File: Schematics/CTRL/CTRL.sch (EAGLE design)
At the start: 50 parts

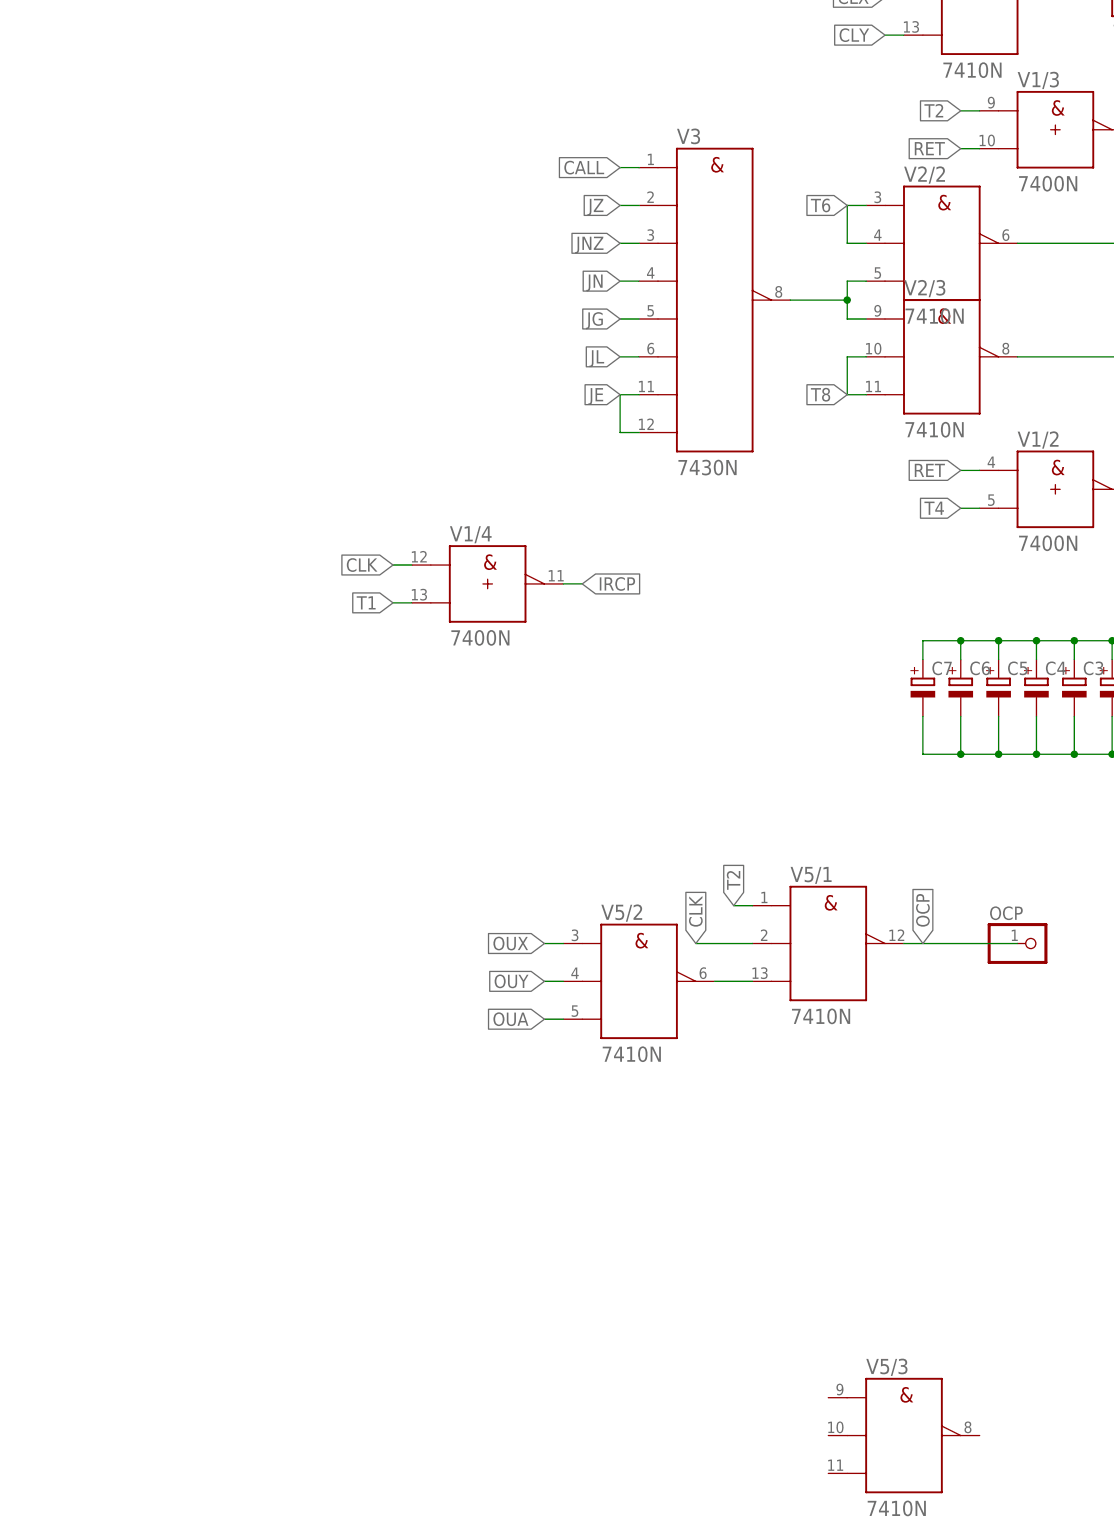
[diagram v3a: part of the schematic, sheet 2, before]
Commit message: Fixed problem with 0xXX
RET wasnt negated, 0xFF and 0xFE started to over heat when T2 was High.
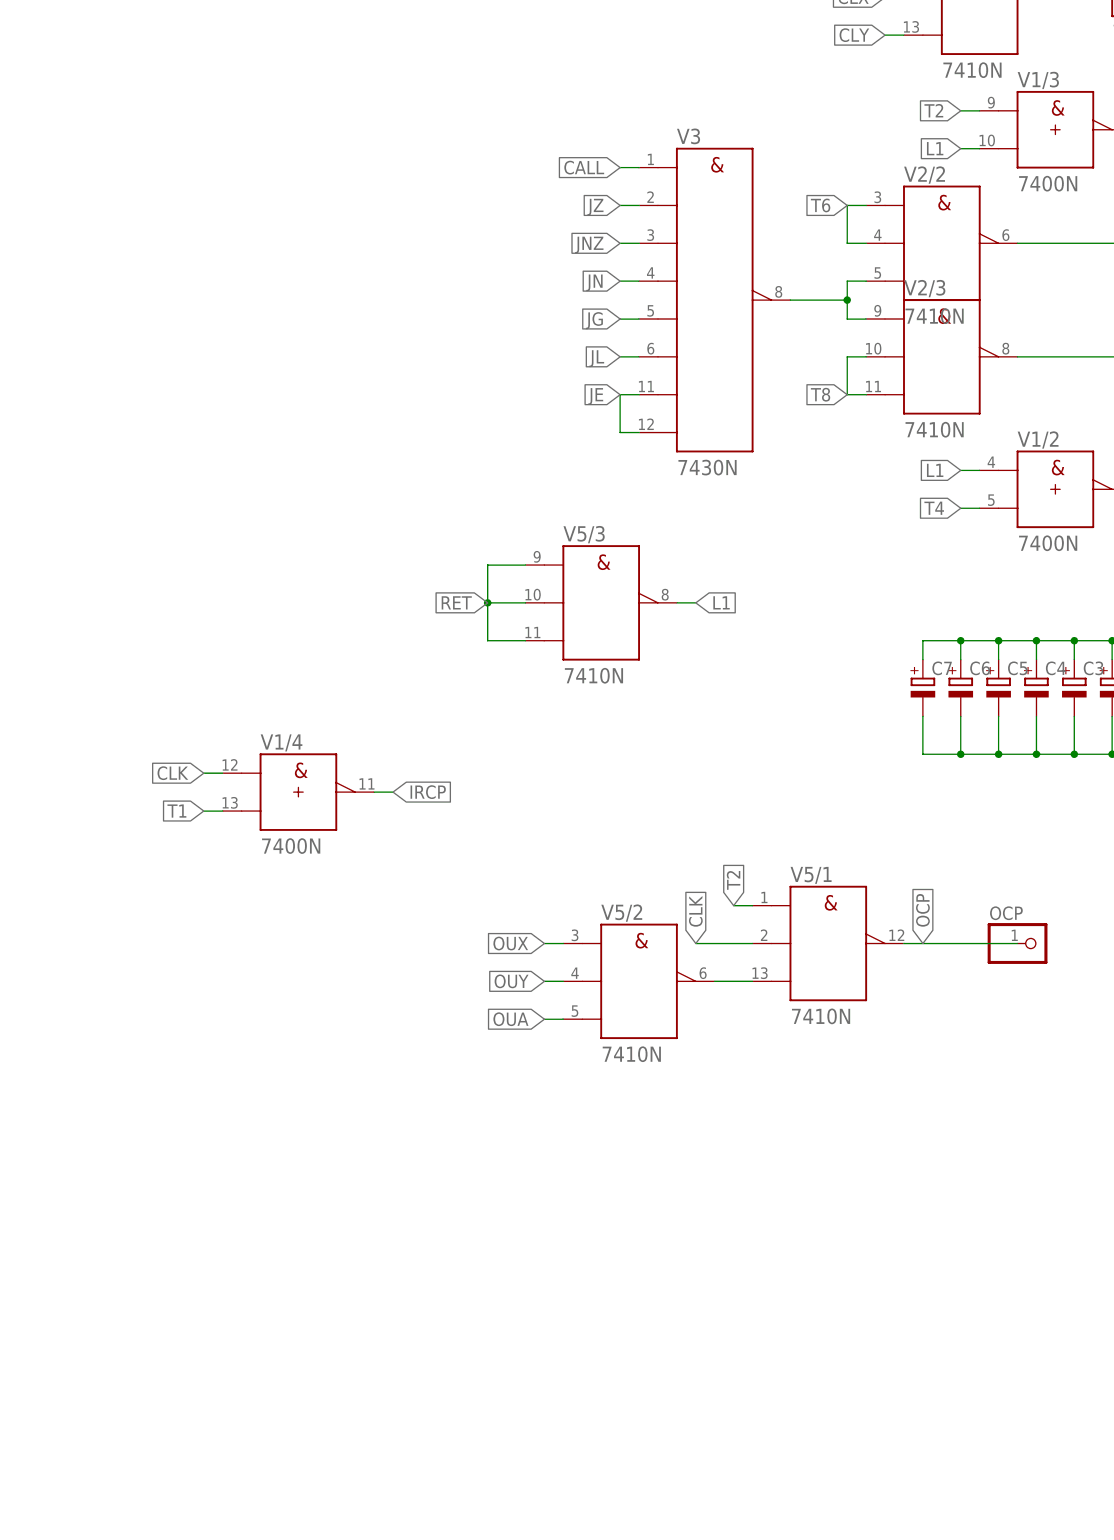
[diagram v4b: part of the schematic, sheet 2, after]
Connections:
- new net L1: V1/2.A, V1/3.B, V5/3.Y
- net RET: now also V5/3.A, V5/3.B, V5/3.C; no longer V1/2.A, V1/3.B
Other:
- moved on the sheet: V1/4, V5/3
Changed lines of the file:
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@@
 <attribute name="VALUE" x="327.66" y="217.805" size="2.032" layer="96"/>
 </instance>
-<instance part="V1" gate="/4" x="256.54" y="165.1" smashed="yes">
-<attribute name="NAME" x="251.46" y="170.815" size="2.032" layer="95"/>
-<attribute name="VALUE" x="251.46" y="156.845" size="2.032" layer="96"/>
+<instance part="V1" gate="/4" x="231.14" y="137.16" smashed="yes">
+<attribute name="NAME" x="226.06" y="142.875" size="2.032" layer="95"/>
+<attribute name="VALUE" x="226.06" y="128.905" size="2.032" layer="96"/>
 </instance>
 <instance part="V2" gate="/1" x="322.58" y="243.84" smashed="yes">
@@
 <attribute name="VALUE" x="271.78" y="100.965" size="2.032" layer="96"/>
 </instance>
-<instance part="V5" gate="/3" x="312.42" y="50.8" smashed="yes">
-<attribute name="NAME" x="307.34" y="59.055" size="2.032" layer="95"/>
-<attribute name="VALUE" x="307.34" y="40.005" size="2.032" layer="96"/>
+<instance part="V5" gate="/3" x="271.78" y="162.56" smashed="yes">
+<attribute name="NAME" x="266.7" y="170.815" size="2.032" layer="95"/>
+<attribute name="VALUE" x="266.7" y="151.765" size="2.032" layer="96"/>
 </instance>
 <instance part="OCP" gate="G$1" x="330.2" y="116.84" smashed="yes">
@@
 <net name="RET" class="0">
 <segment>
-<pinref part="V1" gate="/3" pin="B"/>
-<wire x1="320.04" y1="223.52" x2="322.58" y2="223.52" width="0.1524" layer="91"/>
-<label x="320.04" y="223.52" size="1.778" layer="95" rot="R180" xref="yes"/>
-</segment>
-<segment>
-<pinref part="V1" gate="/2" pin="A"/>
-<wire x1="320.04" y1="180.34" x2="322.58" y2="180.34" width="0.1524" layer="91"/>
-<label x="320.04" y="180.34" size="1.778" layer="95" rot="R180" xref="yes"/>
-</segment>
-<segment>
 <wire x1="63.5" y1="152.4" x2="58.42" y2="152.4" width="0.1524" layer="91"/>
 <pinref part="RAM-OP" gate="A" pin="6"/>
@@
 <pinref part="PC-OP0" gate="A" pin="13"/>
 <label x="129.54" y="147.32" size="1.778" layer="95" xref="yes"/>
+</segment>
+<segment>
+<pinref part="V5" gate="/3" pin="B"/>
+<pinref part="V5" gate="/3" pin="C"/>
+<wire x1="261.62" y1="157.48" x2="256.54" y2="157.48" width="0.1524" layer="91"/>
+<wire x1="256.54" y1="157.48" x2="256.54" y2="162.56" width="0.1524" layer="91"/>
+<pinref part="V5" gate="/3" pin="A"/>
+<wire x1="256.54" y1="162.56" x2="256.54" y2="167.64" width="0.1524" layer="91"/>
+<wire x1="256.54" y1="167.64" x2="261.62" y2="167.64" width="0.1524" layer="91"/>
+<wire x1="261.62" y1="162.56" x2="256.54" y2="162.56" width="0.1524" layer="91"/>
+<junction x="256.54" y="162.56"/>
+<label x="256.54" y="162.56" size="1.778" layer="95" rot="R180" xref="yes"/>
 </segment>
 </net>
@@
 <segment>
 <pinref part="V1" gate="/4" pin="A"/>
-<wire x1="243.84" y1="167.64" x2="246.38" y2="167.64" width="0.1524" layer="91"/>
-<label x="243.84" y="167.64" size="1.778" layer="95" rot="R180" xref="yes"/>
+<wire x1="218.44" y1="139.7" x2="220.98" y2="139.7" width="0.1524" layer="91"/>
+<label x="218.44" y="139.7" size="1.778" layer="95" rot="R180" xref="yes"/>
 </segment>
 <segment>
@@
 <segment>
 <pinref part="V1" gate="/4" pin="B"/>
-<wire x1="243.84" y1="162.56" x2="246.38" y2="162.56" width="0.1524" layer="91"/>
-<label x="243.84" y="162.56" size="1.778" layer="95" rot="R180" xref="yes"/>
+<wire x1="218.44" y1="134.62" x2="220.98" y2="134.62" width="0.1524" layer="91"/>
+<label x="218.44" y="134.62" size="1.778" layer="95" rot="R180" xref="yes"/>
 </segment>
 </net>
@@
 <segment>
 <pinref part="V1" gate="/4" pin="Y"/>
-<wire x1="269.24" y1="165.1" x2="266.7" y2="165.1" width="0.1524" layer="91"/>
-<label x="269.24" y="165.1" size="1.778" layer="95" xref="yes"/>
+<wire x1="243.84" y1="137.16" x2="241.3" y2="137.16" width="0.1524" layer="91"/>
+<label x="243.84" y="137.16" size="1.778" layer="95" xref="yes"/>
 </segment>
 </net>
@@
 </segment>
 </net>
+<net name="L1" class="0">
+<segment>
+<pinref part="V5" gate="/3" pin="Y"/>
+<wire x1="281.94" y1="162.56" x2="284.48" y2="162.56" width="0.1524" layer="91"/>
+<label x="284.48" y="162.56" size="1.778" layer="95" xref="yes"/>
+</segment>
+<segment>
+<pinref part="V1" gate="/2" pin="A"/>
+<wire x1="320.04" y1="180.34" x2="322.58" y2="180.34" width="0.1524" layer="91"/>
+<label x="320.04" y="180.34" size="1.778" layer="95" rot="R180" xref="yes"/>
+</segment>
+<segment>
+<pinref part="V1" gate="/3" pin="B"/>
+<wire x1="322.58" y1="223.52" x2="320.04" y2="223.52" width="0.1524" layer="91"/>
+<label x="320.04" y="223.52" size="1.778" layer="95" rot="R180" xref="yes"/>
+</segment>
+</net>

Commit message: Last (probably) changes to CTRL brd.
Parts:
- removed 0X00, 0XFE, 0XFF: 74245N, 74ttl-din:74245N
- removed ALU-CLK, PC-CLK, PC-CLR, RAM-CLK, REG-CLK: (no value), pinhead:PINHD-1X1
- removed ALU-OP0, REG-OP: (no value), pinhead:PINHD-1X30
- removed ALU-OP1, ALU-T, INC3, INC4: (no value), pinhead:PINHD-1X5
- removed ALU-PS, PC-OP1, PC-PS, RAM-PS, REG-PS: (no value), pinhead:PINHD-1X2
- removed BUS, INC1, INC2, INC7, INC8, RAM-T: (no value), pinhead:PINHD-1X8
- removed C2, C3, C4, C5, C6, C7: (no value), rcl:CPOL-EUE2.5-6
- removed DECODER: (no value), pinhead:PINHD-1X11
- removed INC0: (no value), pinhead:PINHD-1X7
- removed INC5, INC6: (no value), pinhead:PINHD-1X6
- removed PC-OP0: (no value), pinhead:PINHD-1X24
- removed PC-T: (no value), pinhead:PINHD-1X10
- removed RAM-OP: (no value), pinhead:PINHD-1X16
- removed REG-T: (no value), pinhead:PINHD-1X3
- removed TRING: (no value), pinhead:PINHD-1X15
- added ACP, ADD, AND, AOCP, AOE, AOOE, FCP, LC0, LC1, LC2, LC3, LIR0, LIR1, LIR2, LIR3, LIR4, LIR5, LIR6, NOT, OR, PCLR, PHCP, PHOE, PINC, PLCP, PLD, PLOE, POE, RHCP, RLCP, RLD, ROE, RWE, SUB, XCP, XOE, XOR, YCP, YOE: (no value), led:LED5MM
- added ALU: (no value), pinhead:PINHD-2X7
- added BUSIN: (no value), pinhead:PINHD-1X8
- added FLAG, RAM, REG: (no value), pinhead:PINHD-2X3
- added HLT, OCP-P: (no value), pinhead:PINHD-1X1
- added IC1, IC2, IC3, IC4: (no value), memory-nec:28C64C
- added IR: 74273N, 74ttl-din:74273N
- added PC: (no value), pinhead:PINHD-2X4
- added R1, R10, R11, R12, R13, R14, R15, R16, R17, R18, R19, R20, R21, R22, R23, R24, R25, R26, R27, R28, R29, R3, R30, R4, R5, R6, R7, R8, R9: (no value), resistor:R-EU_0204/7
- added R2: (no value), rcl:R-EU_0207/10
- added RC0, RC1, RC2, RC3, RIR0, RIR1, RIR2, RIR3, RIR4, RIR5, RIR6: (no value), rcl:R-EU_0204/7
- added S1: (no value), switch-omron:10-XX
- added V10, V15, V16, V6, V9: 7400N, 74ttl-din:7400N
- added V11, V19: 7408N, 74ttl-din:7408N
- added V12, V13: 7432N, 74ttl-din:7432N
- added V14: 74193N, 74ttl-din:74193N
- added V17, V18: 7404N, 74ttl-din:7404N
- added V8: 74138N, 74ttl-din:74138N
- C1: device rcl:CPOL-EUE2.5-6 -> rcl:C-EU050-035X075
- CLK: device pinhead:PINHD-1X2 -> pinhead:PINHD-1X1
- OCP: device pinhead:PINHD-1X1 -> led:LED5MM
- V1: value 7400N -> 74193N; device 74ttl-din:7400N -> 74ttl-din:74193N
- V2, V5: value 7410N -> 74273N; device 74ttl-din:7410N -> 74ttl-din:74273N
- V3: value 7430N -> 74273N; device 74ttl-din:7430N -> 74ttl-din:74273N
- V4: value 7408N -> 74273N; device 74ttl-din:7408N -> 74ttl-din:74273N
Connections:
- removed net 0X00: 0X001.!G, V1/1.Y
- removed net 0XFE: 0XFE1.!G, V4/2.Y
- removed net 0XFF: 0XFF1.!G, V4/1.Y
- removed net ADA: ALU-OP0.25, INC3.3
- removed net ADI: ALU-OP0.24, INC3.2, PC-OP0.12, RAM-OP.5
- removed net ADV: ALU-OP0.23, INC3.1, PC-OP0.11
- removed net ADX: ALU-OP0.27, INC3.5, REG-OP.22
- removed net ADY: ALU-OP0.26, INC3.4, REG-OP.21
- removed net ANA: ALU-OP0.9, INC7.6
- removed net ANV: ALU-OP0.8, INC7.5, PC-OP0.2
- removed net ANX: ALU-OP0.11, INC7.8, REG-OP.8
- removed net ANY: ALU-OP0.10, INC7.7, REG-OP.7
- removed net CALL: INC1.4, PC-OP0.23, RAM-OP.16, V31.A
- removed net CLA: ALU-OP0.30, INC0.4, V2/1.A
- removed net CLR: PC-CLR.1, TRING.1
- removed net CLX: INC0.6, REG-OP.30, V2/1.B
- removed net CLY: INC0.5, REG-OP.29, V2/1.C
- removed net CMA: ALU-OP0.28, INC1.6
- removed net CMV: INC1.5, PC-OP0.24
- removed net CMX: INC1.8, REG-OP.26
- removed net CMY: INC1.7, REG-OP.25
- removed net IRCP: DECODER.11, V1/4.Y
- removed net JE: INC2.3, PC-OP0.14, RAM-OP.7, V31.G, V31.H
- removed net JG: INC2.4, PC-OP0.16, RAM-OP.8, V31.E
- removed net JL: INC2.5, PC-OP0.15, RAM-OP.9, V31.F
- removed net JN: INC2.6, PC-OP0.17, RAM-OP.10, V31.D
- removed net JNZ: INC2.7, PC-OP0.18, RAM-OP.11, V31.C
- removed net JZ: INC2.8, PC-OP0.19, RAM-OP.12, V31.B
- removed net L1: V1/2.A, V1/3.B, V5/3.Y
- removed net LDA: ALU-OP0.17, INC5.4, PC-OP0.6
- removed net LDAI: ALU-OP0.16, INC5.1, PC-OP0.3, RAM-OP.1
- removed net LDX: INC5.6, PC-OP0.8, REG-OP.18
- removed net LDXI: INC5.3, PC-OP0.5, RAM-OP.3, REG-OP.16
- removed net LDY: INC5.5, PC-OP0.7, REG-OP.17
- removed net LDYI: INC5.2, PC-OP0.4, RAM-OP.2, REG-OP.15
- removed net MAX: ALU-OP0.13, INC6.2, REG-OP.10
- removed net MAY: ALU-OP0.12, INC6.1, REG-OP.9
- removed net MXA: ALU-OP0.15, INC6.5, REG-OP.13
- removed net MXY: INC6.6, REG-OP.14
- removed net MYA: ALU-OP0.14, INC6.3, REG-OP.11
- removed net MYX: INC6.4, REG-OP.12
- removed net NOA: ALU-OP1.2, INC8.2
- removed net NOP: INC0.7
- removed net NOV: ALU-OP1.1, INC8.1, PC-OP1.1
- removed net NOX: ALU-OP1.4, INC8.4, REG-OP.2
- removed net NOY: ALU-OP1.3, INC8.3, REG-OP.1
- removed net ORA: ALU-OP0.5, INC7.2
- removed net ORV: ALU-OP0.4, INC7.1, PC-OP0.1
- removed net ORX: ALU-OP0.7, INC7.4, REG-OP.6
- removed net ORY: ALU-OP0.6, INC7.3, REG-OP.5
- removed net OUA: ALU-OP0.29, INC0.1, V5/2.C
- removed net OUX: INC0.3, REG-OP.28, V5/2.A
- removed net OUY: INC0.2, REG-OP.27, V5/2.B
- removed net RET: INC2.2, PC-OP0.13, RAM-OP.6, V5/3.A, V5/3.B, V5/3.C
- removed net STA: INC1.1, PC-OP0.20, RAM-OP.13
- removed net STX: INC1.3, PC-OP0.22, RAM-OP.15, REG-OP.24
- removed net STY: INC1.2, PC-OP0.21, RAM-OP.14, REG-OP.23
- removed net SUA: ALU-OP0.20, INC4.3
- removed net SUI: ALU-OP0.19, INC4.2, PC-OP0.10, RAM-OP.4
- removed net SUV: ALU-OP0.18, INC4.1, PC-OP0.9
- removed net SUX: ALU-OP0.22, INC4.5, REG-OP.20
- removed net SUY: ALU-OP0.21, INC4.4, REG-OP.19
- removed net T0: PC-T.10, TRING.15
- removed net T1: PC-T.9, TRING.14, V1/4.B
- removed net T10: PC-T.1, TRING.5
- removed net T2: ALU-T.5, PC-T.8, RAM-T.8, REG-T.3, TRING.13, V1/1.A, V1/3.A, V5/1.A
- removed net T3: ALU-T.4, PC-T.7, RAM-T.7, REG-T.2, TRING.12
- removed net T4: ALU-T.3, PC-T.6, RAM-T.6, TRING.11, V1/2.B
- removed net T5: PC-T.5, RAM-T.5, TRING.10
- removed net T6: ALU-T.2, PC-T.4, RAM-T.4, REG-T.1, TRING.9, V2/2.A, V2/2.B
- removed net T7: ALU-T.1, PC-T.3, RAM-T.3, TRING.8
- removed net T8: RAM-T.2, TRING.7, V2/3.B, V2/3.C
- removed net T9: PC-T.2, RAM-T.1, TRING.6
- removed net XOA: ALU-OP0.1, INC8.6
- removed net XOV: ALU-OP1.5, INC8.5, PC-OP1.2
- removed net XOX: ALU-OP0.3, INC8.8, REG-OP.4
- removed net XOY: ALU-OP0.2, INC8.7, REG-OP.3
- new net ACP: ALU.2, V15/4.Y
- new net ACP0: IC1.I/O0, V21.1D
- new net ACP00: R9.2, V10/1.A, V21.1Q
- new net ADD: ALU.6, R15.2, V31.3Q
- new net ADD0: IC1.I/O5, V21.6D
- new net ADD00: R4.2, V15/2.A, V21.6Q
- new net AND: ALU.8, R13.2, V31.5Q
- new net AND0: IC1.I/O7, V21.8D
- new net AND00: R1.2, V15/4.A, V21.8Q
- new net AOCP: ALU.11, V15/3.Y
- new net AOCP0: IC1.I/O3, V21.4D
- new net AOCP00: R6.2, V10/4.A, V21.4Q
- new net AOE: ALU.4, R19.2, V41.7Q
- new net AOE0: IC1.I/O1, V21.2D
- new net AOE00: R8.2, V10/2.A, V21.2Q
- new net AOOE: ALU.12, R18.2, V41.8Q
- new net AOOE0: IC1.I/O4, V21.5D
- new net AOOE00: R5.2, V15/1.A, V21.5Q
- new net C0: IC1.A0, IC2.A0, IC3.A0, IC4.A0, RC0.2, V11.QA
- new net C1: IC1.A1, IC2.A1, IC3.A1, IC4.A1, RC1.2, V11.QB
- new net C2: IC1.A2, IC2.A2, IC3.A2, IC4.A2, RC2.2, V11.QC
- new net C3: IC1.A3, IC2.A3, IC3.A3, IC4.A3, RC3.2, V11.QD
- new net CP: V21.CLK, V31.CLK, V41.CLK, V51.CLK, V9/3.Y
- new net EF: FLAG.4, V11/4.B
- new net FCP: ALU.1, V15/2.Y
- new net FCP0: IC1.I/O2, V21.3D
- new net FCP00: R7.2, V10/3.A, V21.3Q
- new net GF: FLAG.2, V11/3.B
- new net INC: V11.UP, V6/2.A, V9/1.Y
- new net IR0: IC1.A6, IC2.A6, IC3.A6, IC4.A6, IR1.1Q, RIR0.2, V81.A
- new net IR1: IC1.A7, IC2.A7, IC3.A7, IC4.A7, IR1.2Q, RIR1.2, V81.B
- new net IR2: IC1.A8, IC2.A8, IC3.A8, IC4.A8, IR1.3Q, RIR2.2, V81.C
- new net IR3: IC1.A9, IC2.A9, IC3.A9, IC4.A9, IR1.4Q, RIR3.2
- new net IR4: IC1.A10, IC2.A10, IC3.A10, IC4.A10, IR1.5Q, RIR4.2
- new net IR5: IC1.A11, IC2.A11, IC3.A11, IC4.A11, IR1.6Q, RIR5.2
- new net IR6: IC1.A12, IC2.A12, IC3.A12, IC4.A12, IR1.7Q, RIR6.2
- new net LF: FLAG.6, V11/2.B
- new net N$100: V12/4.A, V19/3.Y
- new net N$123: ALU.14
- new net N$13: V141.QA, V9/1.A, V9/1.B, V9/2.A, V9/2.B, V9/3.A
- new net N$14: V18/1.Y, V19/3.A, V19/3.B
- new net N$15: V141.CLR, V141.QB
- new net N$16: NOT.A, R10.1
- new net N$17: R11.1, XOR.A
- new net N$18: IC4.I/O4, V51.5D
- new net N$19: OR.A, R12.1
- new net N$20: AND.A, R13.1
- new net N$21: R14.1, SUB.A
- new net N$22: ADD.A, R15.1
- new net N$23: PHCP.A, R16.1
- new net N$24: PLCP.A, R17.1
- new net N$25: AOOE.A, R18.1
- new net N$26: AOE.A, R19.1
- new net N$27: POE.A, R20.1
- new net N$28: PCLR.A, R21.1
- new net N$29: PHOE.A, R22.1
- new net N$3: LC1.A, RC1.1
- new net N$30: PLOE.A, R23.1
- new net N$31: PLD.A, R24.1
- new net N$32: PINC.A, R25.1
- new net N$33: V11.!CO, V11.CLR
- new net N$34: V18/2.Y, V19/4.A
- new net N$35: V17/6.Y, V19/2.A
- new net N$36: V17/5.Y, V19/1.A
- new net N$37: V11/4.A, V17/4.Y
- new net N$38: V11/3.A, V17/3.Y
- new net N$39: V11/2.A, V17/2.Y
- new net N$4: LC0.A, RC0.1
- new net N$41: V17/1.A, V81.Y0
- new net N$42: V17/2.A, V81.Y1
- new net N$43: V17/3.A, V81.Y2
- new net N$44: V17/4.A, V81.Y3
- new net N$45: V17/5.A, V81.Y4
- new net N$46: V17/6.A, V81.Y5
- new net N$47: V18/1.A, V81.Y6
- new net N$48: V18/2.A, V81.Y7
- new net N$49: R26.1, RLD.A
- new net N$5: ACP.A, R1.1
- new net N$50: R27.1, YOE.A
- new net N$51: R28.1, XOE.A
- new net N$52: R29.1, ROE.A
- new net N$53: R30.1, RWE.A
- new net N$54: V13/3.Y, V18/3.A
- new net N$57: LIR0.A, RIR0.1
- new net N$58: LIR1.A, RIR1.1
- new net N$59: LIR2.A, RIR2.1
- new net N$60: LIR3.A, RIR3.1
- new net N$65: LIR4.A, RIR4.1
- new net N$7: FCP.A, R4.1
- new net N$72: LIR5.A, RIR5.1
- new net N$73: LIR6.A, RIR6.1
- new net N$77: V12/4.Y, V13/2.B
- new net N$78: V12/3.Y, V13/2.A
- new net N$79: V12/1.Y, V13/1.A
- new net N$8: R5.1, XCP.A
- new net N$80: V12/2.Y, V13/1.B
- new net N$85: V13/1.Y, V13/3.A
- new net N$86: V13/2.Y, V13/3.B
- new net N$90: V11/2.Y, V12/1.A, V12/1.B
- new net N$91: V11/3.Y, V12/2.A
- new net N$92: V11/4.Y, V12/2.B
- new net N$93: V12/3.A, V19/1.Y
- new net N$94: V12/3.B, V19/2.Y
- new net N$97: ALU.5
- new net N$98: ALU.3
- new net N$99: V12/4.B, V19/4.Y
- new net NCLK: V10/1.B, V10/2.B, V10/3.B, V10/4.B, V15/1.B, V15/2.B, V15/3.B, V15/4.B, V16/1.B, V16/2.B, V6/1.A, V6/2.Y, V9/4.A
- new net NG: FLAG.3, V19/2.B
- new net NOT: ALU.9, R10.2, V31.8Q
- new net NOT0: IC2.I/O2, V31.3D
- new net OCP0: IC3.I/O7, V41.8D
- new net OE: IC1.!OE, IC2.!OE, IC3.!OE, IC4.!OE, V9/2.Y
- new net OF: FLAG.5, V19/1.B
- new net OR: ALU.10, R12.2, V31.6Q
- new net OR0: IC2.I/O0, V31.1D
- new net OR00: R17.2, V16/1.A, V31.1Q
- new net PCLD: C1.1, IR1.!CLR, R2.1, S1.S, S1.S1, V11.!LOAD, V141.!LOAD
- new net PCLR: PC.2, R21.2, V41.5Q
- new net PCLR0: IC3.I/O0, V41.1D
- new net PHCP: PC.5, V16/2.Y
- new net PHCP0: IC2.I/O4, V31.5D
- new net PHOE: PC.6, R22.2, V41.4Q
- new net PHOE0: IC2.I/O6, V31.7D
- new net PINC: PC.4, R25.2, V41.1Q
- new net PINC0: IC2.I/O7, V31.8D
- new net PLCP: PC.1, V16/1.Y
- new net PLCP0: IC2.I/O3, V31.4D
- new net PLD: PC.3, R24.2, V41.2Q
- new net PLD0: IC3.I/O1, V81.G1
- new net PLD1: V18/3.Y, V41.2D
- new net PLOE: PC.8, R23.2, V41.3Q
- new net PLOE0: IC2.I/O5, V31.6D
- new net POE: PC.7, R20.2, V41.6Q
- new net POE0: IC3.I/O2, V41.3D
- new net RHCP: RAM.2, V10/2.Y
- new net RHCP0: IC3.I/O4, V41.5D
- new net RL: IR1.CLK, V9/4.Y
- new net RLCP: RAM.1, V10/3.Y
- new net RLCP0: IC3.I/O3, V41.4D
- new net RLD: R26.2, V51.5Q, V9/4.B
- new net ROE: R29.2, RAM.4, V51.2Q
- new net ROE0: IC3.I/O6, V41.7D
- new net RWE: RAM.3, V6/1.Y
- new net RWE0: IC3.I/O5, V41.6D
- new net RWE000: R30.2, V51.1Q, V6/1.B
- new net SUB: ALU.13, R14.2, V31.4Q
- new net SUB0: IC1.I/O6, V21.7D
- new net SUB00: R3.2, V15/3.A, V21.7Q
- new net XCP: REG.1, V15/1.Y
- new net XCP0: IC4.I/O0, V51.1D
- new net XOE: R28.2, REG.3, V51.3Q
- new net XOE0: IC4.I/O1, V51.2D
- new net XOR: ALU.7, R11.2, V31.7Q
- new net XOR0: IC2.I/O1, V31.2D
- new net XOR00: R16.2, V16/2.A, V31.2Q
- new net YCP: REG.2, V10/4.Y
- new net YCP0: IC4.I/O2, V51.3D
- new net YOE: R27.2, REG.4, V51.4Q
- new net YOE0: IC4.I/O3, V51.4D
- new net ZF: FLAG.1, V19/4.B
- net B0: now also BUSIN.1, IR1.1D; no longer 0X001.B1, 0XFE1.B1, 0XFF1.B1, BUS.8, DECODER.3
- net B1: now also BUSIN.2, IR1.2D; no longer 0X001.B2, 0XFE1.B2, 0XFF1.B2, BUS.7, DECODER.4
- net B2: now also BUSIN.3, IR1.3D; no longer 0X001.B3, 0XFE1.B3, 0XFF1.B3, BUS.6, DECODER.5
- net B3: now also BUSIN.4, IR1.4D; no longer 0X001.B4, 0XFE1.B4, 0XFF1.B4, BUS.5, DECODER.6
- net B4: now also BUSIN.5, IR1.5D; no longer 0X001.B5, 0XFE1.B5, 0XFF1.B5, BUS.4, DECODER.7
- net B5: now also BUSIN.6, IR1.6D; no longer 0X001.B6, 0XFE1.B6, 0XFF1.B6, BUS.3, DECODER.8
- net B6: now also BUSIN.7, IR1.7D; no longer 0X001.B7, 0XFE1.B7, 0XFF1.B7, BUS.2, DECODER.9
- net B7: now also BUSIN.8, IR1.8D; no longer 0X001.B8, 0XFE1.B8, 0XFF1.B8, BUS.1, DECODER.10
- net CLK: now also CLK.1, V141.UP, V6/2.B, V9/3.B; no longer ALU-CLK.1, CLK.2, PC-CLK.1, RAM-CLK.1, REG-CLK.1, TRING.2, V1/4.A, V5/1.B
- net GND: now also ACP.C, ADD.C, AND.C, AOCP.C, AOE.C, AOOE.C, C1.2, CLK-PS.2, FCP.C, IC1.!CE, IC1.A4, IC1.A5, IC1.GND, IC2.!CE, IC2.A4, IC2.A5, IC2.GND, IC3.!CE, IC3.A4, IC3.A5, IC3.GND, IC4.!CE, IC4.A4, IC4.A5, IC4.GND, IR/-UB.-UB, LC0.C, LC1.C, LC2.C, LC3.C, LIR0.C, LIR1.C, LIR2.C, LIR3.C, LIR4.C, LIR5.C, LIR6.C, NOT.C, OCP.C, OR.C, PCLR.C, PHCP.C, PHOE.C, PINC.C, PLCP.C, PLD.C, PLOE.C, POE.C, PS.2, RHCP.C, RLCP.C, RLD.C, ROE.C, RWE.C, S1.P, S1.P1, SUB.C, V10/-UB.-UB, V11.A, V11.B, V11.C, V11.D, V11.DOWN, V11/-UB.-UB, V12/-UB.-UB, V13/-UB.-UB, V14/-UB.-UB, V141.A, V141.B, V141.C, V141.D, V141.DOWN, V15/-UB.-UB, V16/-UB.-UB, V17/-UB.-UB, V18/-UB.-UB, V19/-UB.-UB, V6/-UB.-UB, V8/-UB.-UB, V81.!G2A, V81.!G2B, V9/-UB.-UB, XCP.C, XOE.C, XOR.C, YCP.C, YOE.C; no longer 0X00/-UB.-UB, 0X001.A1, 0X001.A2, 0X001.A3, 0X001.A4, 0X001.A5, 0X001.A6, 0X001.A7, 0X001.A8, 0XFE/-UB.-UB, 0XFE1.A1, 0XFF/-UB.-UB, ALU-PS.1, C1.-, C2.-, C3.-, C4.-, C5.-, C6.-, C7.-, CLK-PS.1, DECODER.2, PC-PS.1, PS.1, RAM-PS.1, REG-PS.1, TRING.3
- net HLT: now also HLT.1, IR1.8Q; no longer CLK.1, INC2.1
- net N$1: now also LC3.A, RC3.1; no longer V1/1.B, V2/1.Y
- net N$10: now also R7.1, RLCP.A; no longer V1/2.Y, V4/2.B
- net N$11: now also R8.1, RHCP.A; no longer V2/2.Y, V4/1.B
- net N$12: now also OCP.A, R9.1; no longer V1/3.Y, V4/1.A
- net N$2: now also LC2.A, RC2.1; no longer V2/2.C, V2/3.A, V31.Y
- net N$6: now also AOCP.A, R3.1; no longer V5/1.C, V5/2.Y
- net N$9: now also R6.1, YCP.A; no longer V2/3.Y, V4/2.A
- net OCP: now also OCP-P.1, V10/1.Y; no longer OCP.1, V5/1.Y
- net VCC: now also CLK-PS.1, IC1.!WE, IC1.VCC, IC2.!WE, IC2.VCC, IC3.!WE, IC3.VCC, IC4.!WE, IC4.VCC, IR/+UB.+UB, PS.1, R2.2, V10/+UB.+UB, V11/+UB.+UB, V12/+UB.+UB, V13/+UB.+UB, V14/+UB.+UB, V15/+UB.+UB, V16/+UB.+UB, V17/+UB.+UB, V18/+UB.+UB, V19/+UB.+UB, V21.!CLR, V31.!CLR, V41.!CLR, V51.!CLR, V6/+UB.+UB, V8/+UB.+UB, V9/+UB.+UB; no longer 0X00/+UB.+UB, 0X001.DIR, 0XFE/+UB.+UB, 0XFE1.A2, 0XFE1.A3, 0XFE1.A4, 0XFE1.A5, 0XFE1.A6, 0XFE1.A7, 0XFE1.A8, 0XFE1.DIR, 0XFF/+UB.+UB, 0XFF1.A1, 0XFF1.A2, 0XFF1.A3, 0XFF1.A4, 0XFF1.A5, 0XFF1.A6, 0XFF1.A7, 0XFF1.A8, 0XFF1.DIR, ALU-PS.2, C1.+, C2.+, C3.+, C4.+, C5.+, C6.+, C7.+, CLK-PS.2, DECODER.1, PC-PS.2, PS.2, RAM-PS.2, REG-PS.2, TRING.4
